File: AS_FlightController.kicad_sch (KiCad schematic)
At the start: 53 parts, among them J1 USB_C_Receptacle_USB2.0, J2 Conn_01x04_Pin, J3 Conn_01x02_Pin, J4 Conn_01x02_Pin, SW1 SW_SPDT, U1 STM32H753ZIT6, U2 AMS1117-3.3, U3 USBLC6-2SC6, U4 ICM-42670-P, Y1 25MHZ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

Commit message: Changing to breakout
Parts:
- removed C25: 10n, symbol Device:C
- removed C26: 0.1u, symbol Device:C
- removed C27: 2.2u, symbol Device:C
- removed J2: Conn_01x04_Pin, symbol Connector:Conn_01x04_Pin
- removed J3, J4: Conn_01x02_Pin, symbol Connector:Conn_01x02_Pin
- removed U4: ICM-42670-P, LGA14_2.5X3X0.76_IVS, symbol ICM-42670-P:ICM-42670-P
- added J2, J3, J4, J5: Conn_01x13_Pin, symbol Connector:Conn_01x13_Pin
- added R10, R11, R12, R13, R14: 4.7K, symbol Device:R
- R6: value 2.2K -> 100K
- R7: value 2.2K -> 4.7K
- R8, R9: value 10K -> 4.7K
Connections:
- net +3.3V: now also R6.1, R7.1, R10.1, R11.1, R12.1, R13.1, R14.1
- net I2C1_SCL: now also U1.139 (PB8), J5.11 (Pin_11)
- net I2C1_SDA: now also R8.2, U1.137 (PB7), J5.10 (Pin_10); no longer R6.2
- net I2C2_SCL: now also J5.9 (Pin_9)
- net I2C2_SDA: now also J5.8 (Pin_8), R10.2; no longer R8.2
- net SWCLK: now also J2.7 (Pin_7), J5.12 (Pin_12)
- net SWDIO: now also R6.2, J2.6 (Pin_6), J5.13 (Pin_13)
- net UART7_TX: now also U1.59 (PE8); no longer U1.19 (PF7)
- net at U1.136 (PB6): no longer R7.1
- net SPI4_SCK: now reaches U1.1 (PE2)
- net SPI4_SCK: now also J4.2 (Pin_2)
- net I2C3_SCL: now reaches U1.100 (PA8)
- net I2C3_SCL: now also J5.7 (Pin_7), R11.2
- net SPI3_SCK: now reaches U1.111 (PC10)
- net SPI3_SCK: now also J4.5 (Pin_5)
- net SPI3_MISO: now reaches U1.112 (PC11)
- net SPI3_MISO: now also J4.7 (Pin_7)
- net SDMMC2_CK: now reaches U1.122 (PD6)
- net SDMMC2_CMD: now reaches U1.123 (PD7)
- net SDMMC2_D2: now reaches U1.126 (PG11)
- net SPI6_MISO: now reaches U1.127 (PG12)
- net SPI6_MISO: now also J2.10 (Pin_10)
- net SPI6_SCK: now reaches U1.128 (PG13)
- net SPI6_SCK: now also J2.8 (Pin_8)
- net SPI6_MOSI: now reaches U1.129 (PG14)
- net SPI6_MOSI: now also J2.9 (Pin_9)
- net SDMMC2_D3: now reaches U1.134 (PB4)
- net SPI5_MISO: now reaches U1.20 (PF8)
- net SPI5_MISO: now also J2.13 (Pin_13)
- net SPI5_MOSI: now reaches U1.21 (PF9)
- net SPI5_MOSI: now also J2.12 (Pin_12)
- net SPI2_MOSI: now reaches U1.27 (PC1)
- net SPI2_MOSI: now also J4.9 (Pin_9)
- net SPI2_MISO: now reaches U1.28 (PC2_C)
- net SPI2_MISO: now also J4.10 (Pin_10)
- net SPI4_MISO: now reaches U1.4 (PE5)
- net SPI4_MISO: now also J4.4 (Pin_4)
- net SPI1_SCK: now reaches U1.41 (PA5)
- net SPI1_SCK: now also J4.11 (Pin_11)
- net SPI1_MISO: now reaches U1.42 (PA6)
- net SPI1_MISO: now also J4.13 (Pin_13)
- net SPI1_MOSI: now reaches U1.43 (PA7)
- net SPI1_MOSI: now also J4.12 (Pin_12)
- net GPIO_PWM_1: now reaches U1.44 (PC4)
- net GPIO_PWM_2: now reaches U1.45 (PC5)
- net GPIO_PWM_3: now reaches U1.46 (PB0)
- net GPIO_PWM_4: now reaches U1.47 (PB1)
- net SPI3_MOSI: now reaches U1.48 (PB2)
- net SPI3_MOSI: now also J4.6 (Pin_6)
- net SPI4_MOSI: now reaches U1.5 (PE6)
- net SPI4_MOSI: now also J4.3 (Pin_3)
- net I2C4_SCL: now reaches U1.54 (PF14)
- net I2C4_SCL: now also J5.5 (Pin_5), R13.2
- net I2C4_SDA: now reaches U1.55 (PF15)
- net I2C4_SDA: now also J5.4 (Pin_4), R14.2
- net SPI2_SCK: now reaches U1.69 (PB10)
- net SPI2_SCK: now also J4.8 (Pin_8)
- net UART5_RX: now reaches U1.73 (PB12)
- net UART5_TX: now reaches U1.74 (PB13)
- net SDMMC2_D0: now reaches U1.75 (PB14)
- net SDMMC2_D1: now reaches U1.76 (PB15)
- net I2C3_SDA: now reaches U1.99 (PC9)
- net I2C3_SDA: now also J5.6 (Pin_6), R12.2
- net IMU_FSYNC: no longer names the net of U1.86 (PD15)
- net IMU_INT1: no longer names the net of U1.82 (PD13)
- net IMU_INT2: no longer names the net of U1.85 (PD14)
- new net SPI5_SCK: J2.11 (Pin_11), U1.19 (PF7)
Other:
- note removed: "Gives I2C Address of 0x69"
- note removed: "IMU_6_Axis"

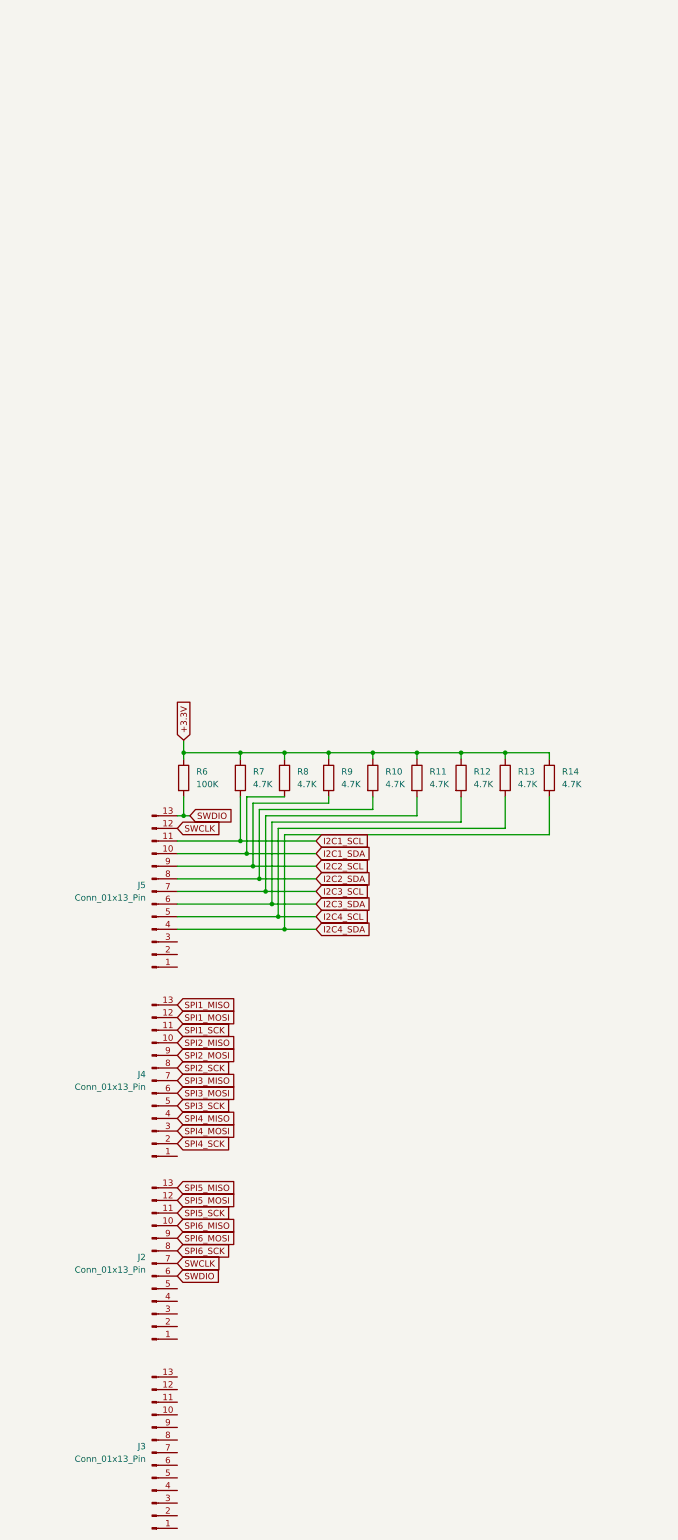
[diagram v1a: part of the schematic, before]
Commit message: Adding connectors
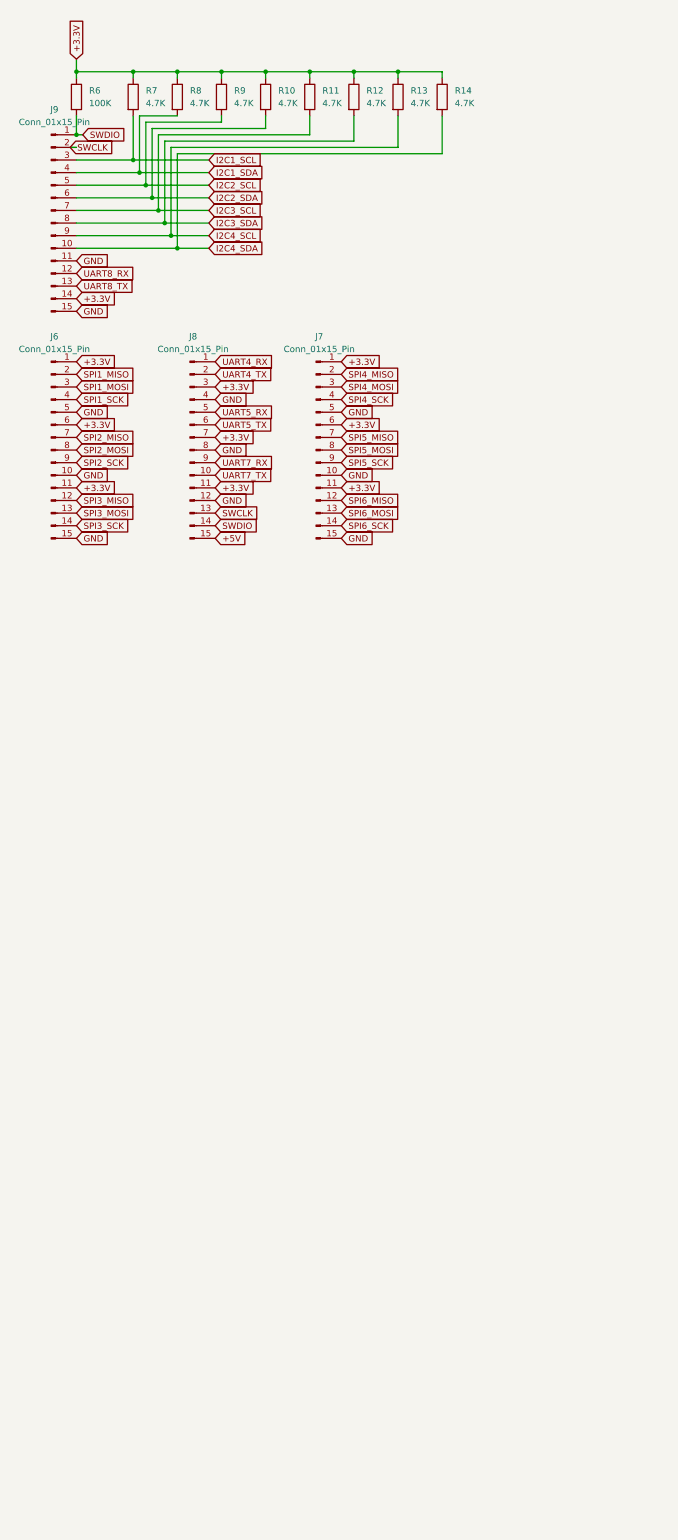
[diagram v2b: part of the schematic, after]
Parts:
- removed J2, J3, J4, J5: Conn_01x13_Pin, symbol Connector:Conn_01x13_Pin
- added J6, J7, J8, J9: Conn_01x15_Pin, symbol Connector:Conn_01x15_Pin
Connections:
- net +3.3V: now also J6.1 (Pin_1), J6.11 (Pin_11), J6.6 (Pin_6), J7.1 (Pin_1), J7.11 (Pin_11), J7.6 (Pin_6), J8.11 (Pin_11), J8.3 (Pin_3), J8.7 (Pin_7), J9.14 (Pin_14)
- net +5V: now also J8.15 (Pin_15)
- net GND: now also J6.10 (Pin_10), J6.15 (Pin_15), J6.5 (Pin_5), J7.10 (Pin_10), J7.15 (Pin_15), J7.5 (Pin_5), J8.12 (Pin_12), J8.4 (Pin_4), J8.8 (Pin_8), J9.11 (Pin_11), J9.15 (Pin_15)
- net I2C1_SCL: now also J9.3 (Pin_3)
- net I2C1_SDA: now also J9.4 (Pin_4)
- net I2C2_SCL: now also J9.5 (Pin_5)
- net I2C2_SDA: now also J9.6 (Pin_6)
- net I2C3_SCL: now also J9.7 (Pin_7)
- net I2C3_SDA: now also J9.8 (Pin_8)
- net I2C4_SCL: now also J9.9 (Pin_9)
- net I2C4_SDA: now also J9.10 (Pin_10)
- net SPI1_MISO: now also J6.2 (Pin_2)
- net SPI1_MOSI: now also J6.3 (Pin_3)
- net SPI1_SCK: now also J6.4 (Pin_4)
- net SPI2_MISO: now also J6.7 (Pin_7)
- net SPI2_MOSI: now also J6.8 (Pin_8)
- net SPI2_SCK: now also J6.9 (Pin_9)
- net SPI3_MISO: now also J6.12 (Pin_12)
- net SPI3_MOSI: now also J6.13 (Pin_13)
- net SPI3_SCK: now also J6.14 (Pin_14)
- net SPI4_MISO: now also J7.2 (Pin_2)
- net SPI4_MOSI: now also J7.3 (Pin_3)
- net SPI4_SCK: now also J7.4 (Pin_4)
- net SPI5_MISO: now also J7.7 (Pin_7)
- net SPI5_MOSI: now also J7.8 (Pin_8)
- net SPI5_SCK: now also J7.9 (Pin_9)
- net SPI6_MISO: now also J7.12 (Pin_12)
- net SPI6_MOSI: now also J7.13 (Pin_13)
- net SPI6_SCK: now also J7.14 (Pin_14)
- net SWCLK: now also J8.13 (Pin_13), J9.2 (Pin_2)
- net SWDIO: now also J8.14 (Pin_14), J9.1 (Pin_1)
- net UART4_RX: now also J8.1 (Pin_1)
- net UART4_TX: now also J8.2 (Pin_2)
- net UART5_RX: now also J8.5 (Pin_5)
- net UART5_TX: now also J8.6 (Pin_6)
- net UART7_RX: now also J8.9 (Pin_9)
- net UART7_TX: now also J8.10 (Pin_10)
- net UART8_RX: now also J9.12 (Pin_12)
- net UART8_TX: now also J9.13 (Pin_13)
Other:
- moved on the sheet: R10, R11, R12, R13, R14, R6, R7, R8, R9

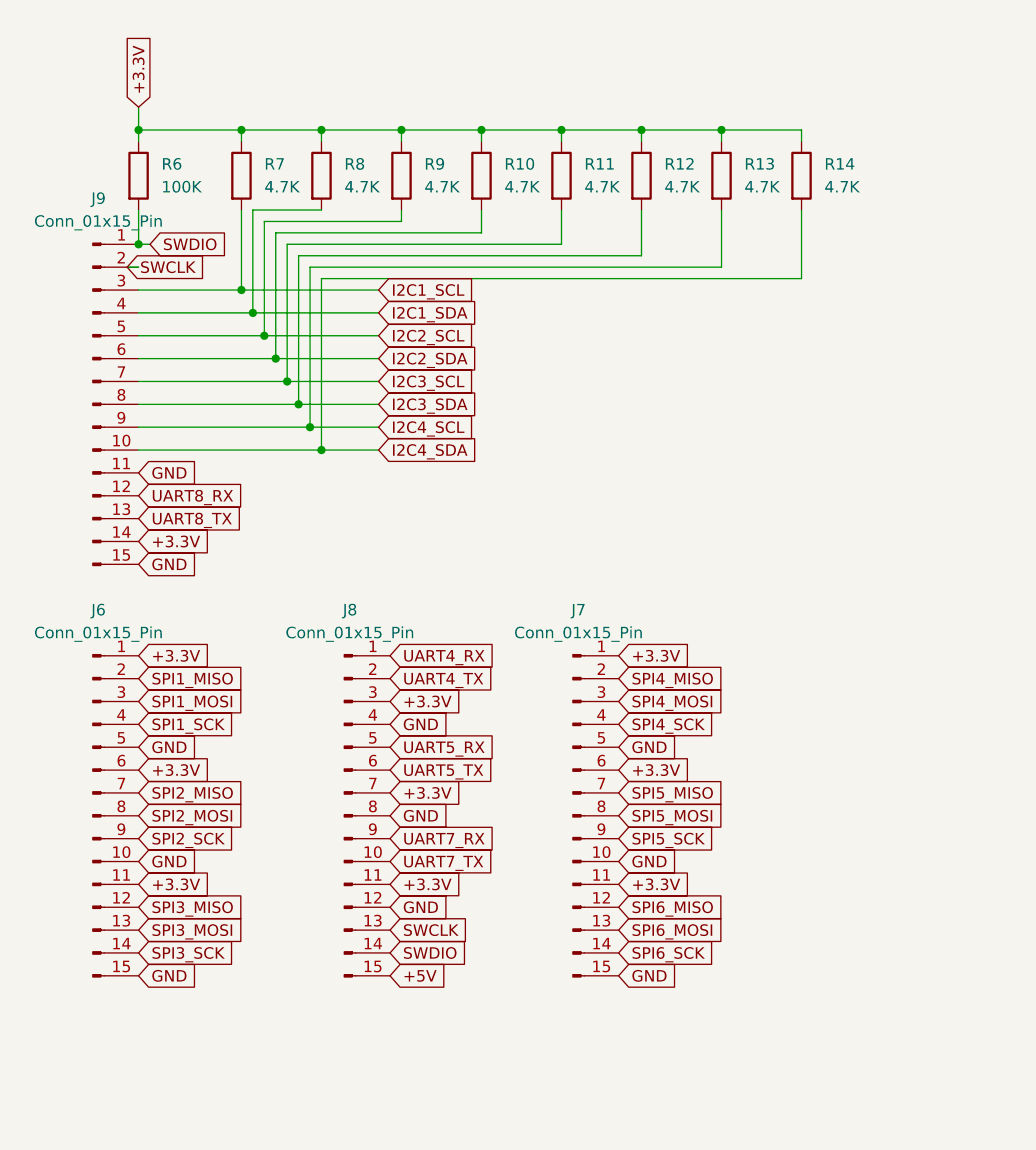
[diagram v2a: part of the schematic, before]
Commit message: Removing connectors
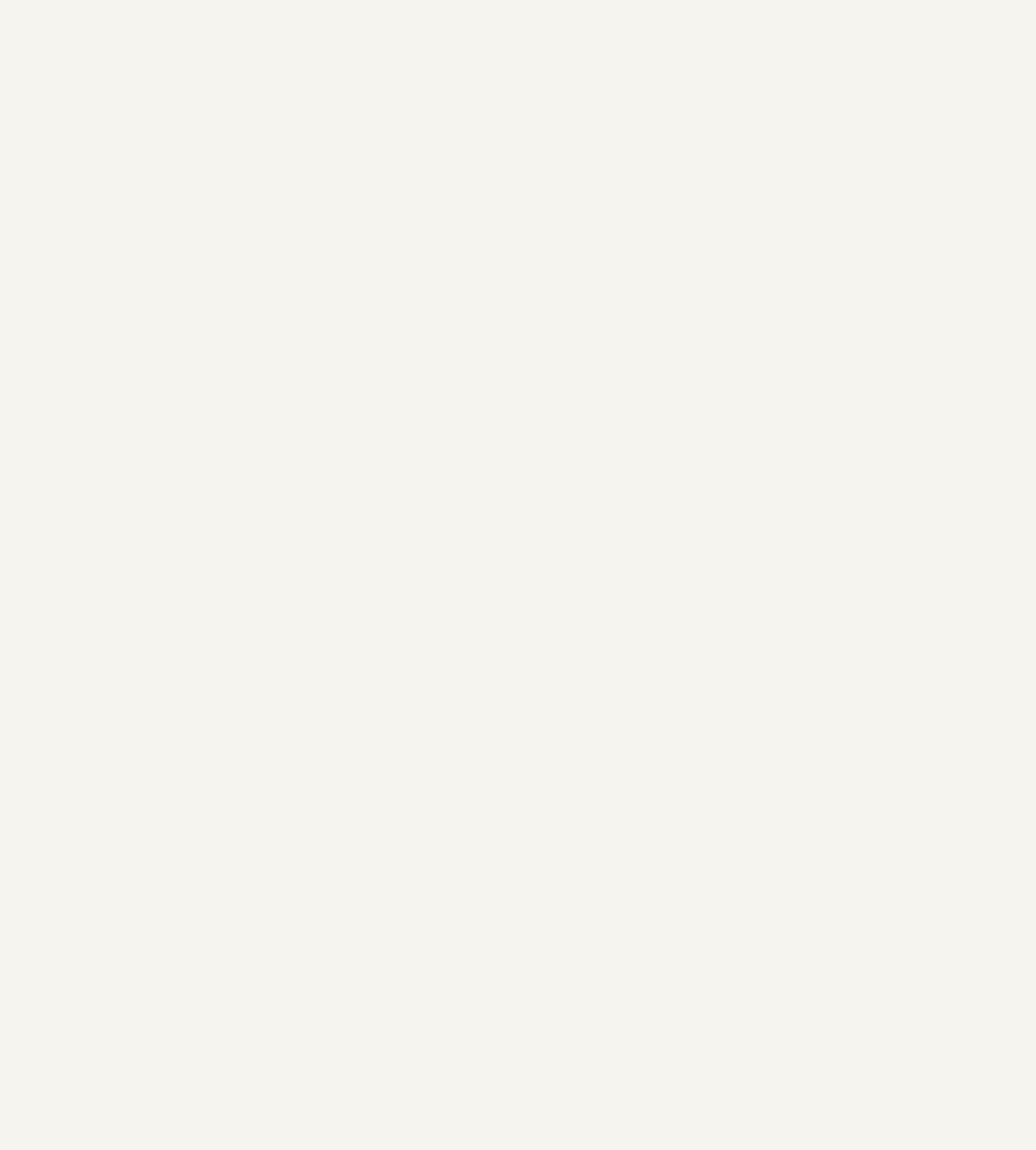
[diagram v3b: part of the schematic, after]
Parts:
- removed J6, J7, J8, J9: Conn_01x15_Pin, symbol Connector:Conn_01x15_Pin
- removed R10, R11, R12, R13, R14, R7, R8, R9: 4.7K, symbol Device:R
- removed R6: 100K, symbol Device:R
